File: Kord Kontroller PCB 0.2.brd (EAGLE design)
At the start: 242.5 x 100 mm, 190 parts, among them IC2 74HCT1G125DBV, IC4 ATSAMD51G_TQFN48, J1 MIDIOUTB, J2 MIDIOUTA, SW1 SPST_TACT-KMR2, U1 AP2112K-3.3, U2 ATSAMD51J19A-AUT, X3 microUSB

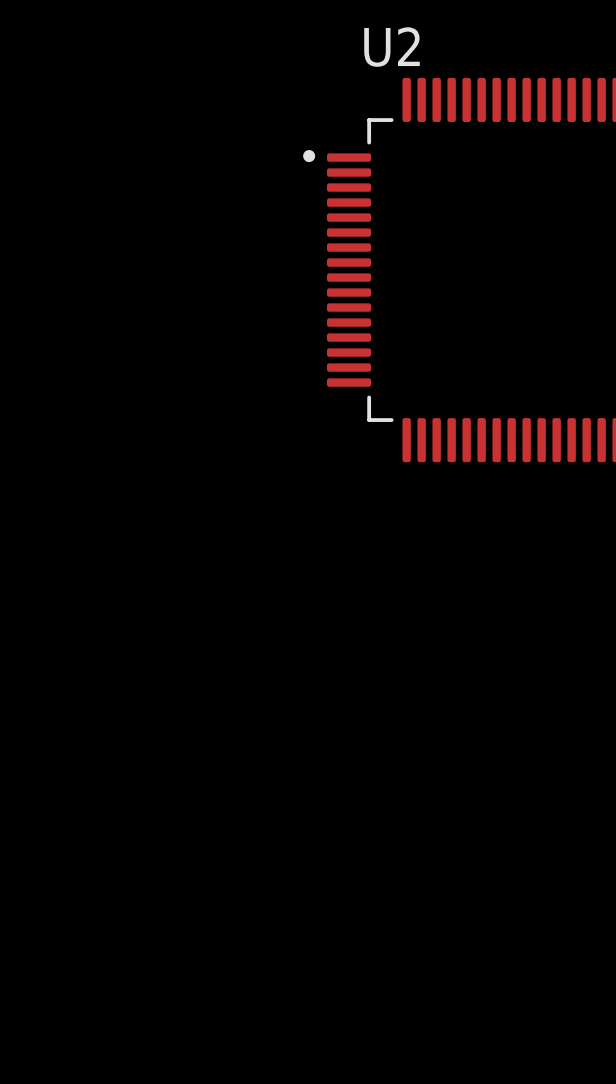
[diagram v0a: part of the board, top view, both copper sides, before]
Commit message: Added lines to new 64-QFN part
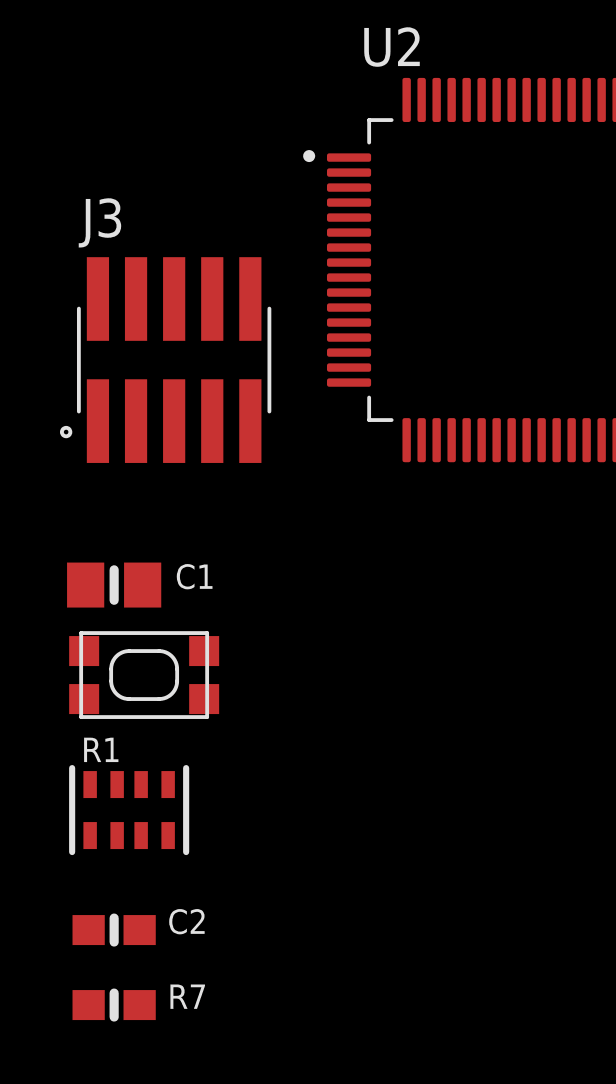
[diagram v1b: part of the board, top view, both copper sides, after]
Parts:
- added C1: 10uF, microbuilder:0805-NO
- added C2: 0.1uF, microbuilder:0603-NO
- added J3: FTSH-105-01-L-DV-KJ, FTSH-105-01-L-DV-K:SAMTEC_FTSH-105-01-L-DV-K
- added R1: 10K, microbuilder:RESPACK_4X0603
- added R7: 10K, microbuilder:0603-NO
- added SW2: SPST_TACT-KMR2, adafruit:KMR2
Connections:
- removed net VDDANA: U2.8
- removed net VDDIO: U2.21, U2.34, U2.48, U2.56
- new net NRESET: C2.2, J3.10, R1.1, SW2.1, SW2.3, U2.52
- new net SWDCLK: J3.4, R7.1, U2.57
- new net SWO: J3.6, U2.59
- new net VDDCORE1: C1.1, U2.53
- net 3.3V: now also J3.1, R1.8, R7.2, U2.21, U2.34, U2.48, U2.56
- net AVDD: now also U2.8
- net COL0: now also U2.1
- net COL1: now also U2.2
- net COL10: now also U2.38
- net COL11: now also U2.41
- net COL12: now also U2.42
- net COL13: now also U2.43
- net COL14: now also U2.44
- net COL2: now also U2.3
- net COL3: now also U2.4
- net COL4: now also U2.13
- net COL5: now also U2.14
- net COL6: now also U2.15
- net COL7: now also U2.35
- net COL8: now also U2.36
- net COL9: now also U2.37
- net D+: now also U2.46
- net D-: now also U2.45
- net GND: now also C1.2, C2.1, J3.3, J3.5, J3.9, SW2.2, SW2.4
- net INT: now also U2.16
- net LEVELSHIFT_3V: now also U2.51
- net MIDIOUTA: now also U2.29
- net MIDIOUTB: now also U2.30
- net ROW0: now also U2.64
- net ROW1: now also U2.63
- net ROW2: now also U2.62
- net ROW3: now also U2.23
- net ROW4: now also U2.24
- net SWDIO: now also J3.2, U2.58
- net VDDCORE: no longer U2.53

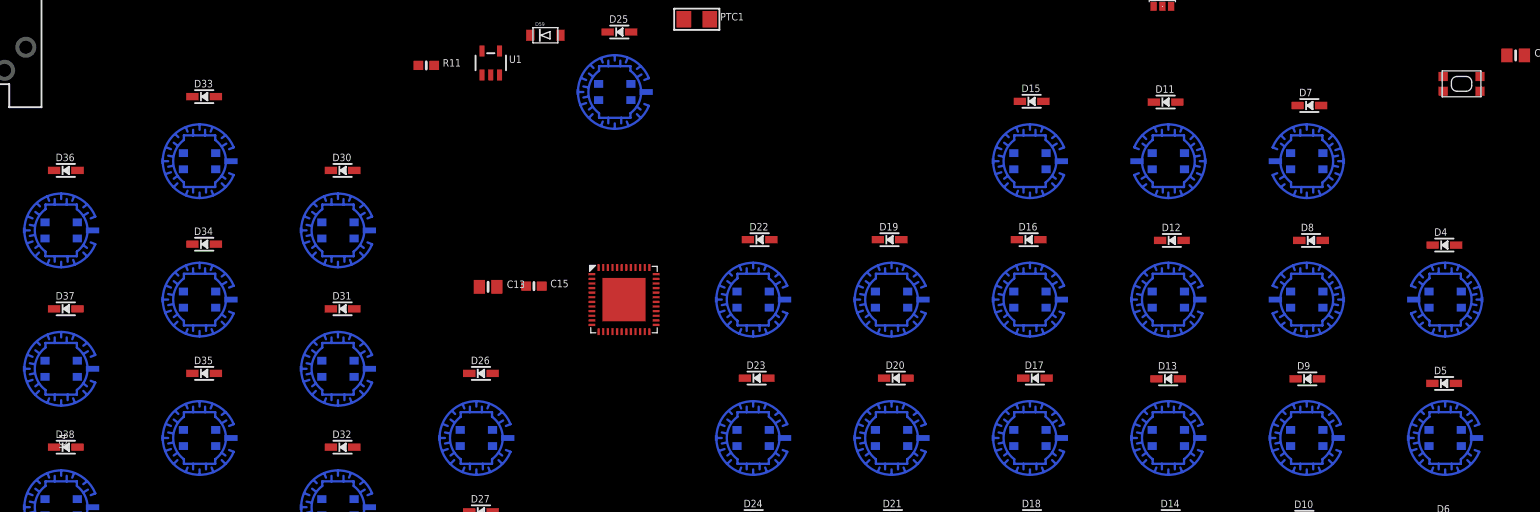
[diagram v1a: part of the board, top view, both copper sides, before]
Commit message: Deleted TQFN8 pin package for 64 pin package
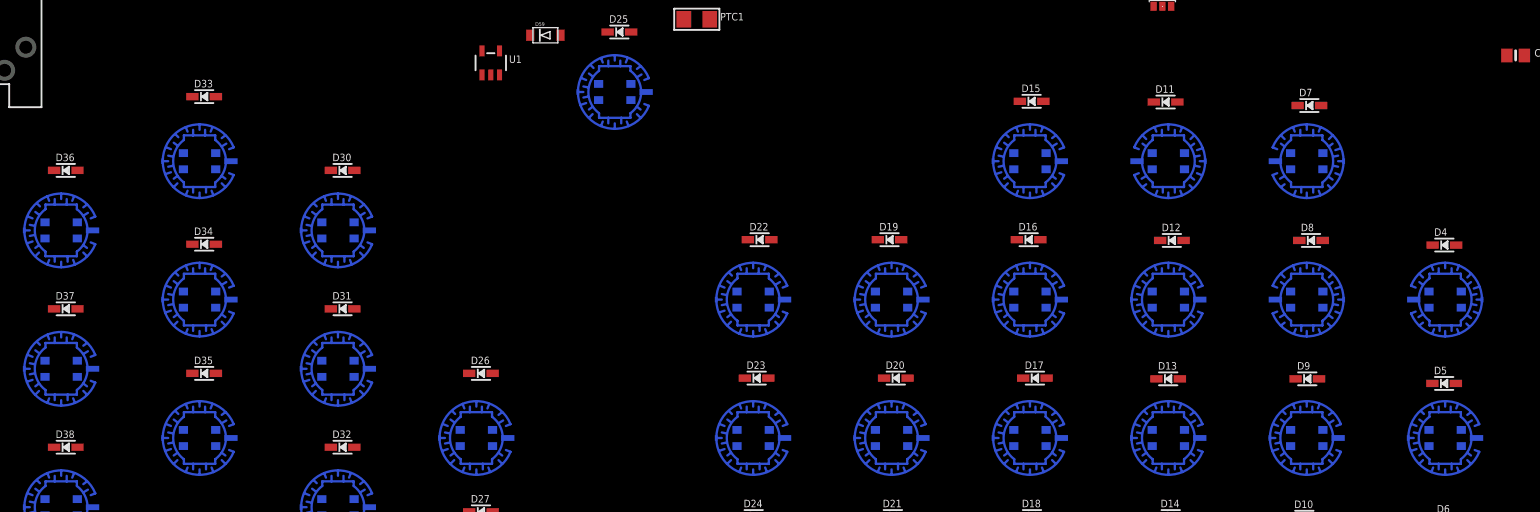
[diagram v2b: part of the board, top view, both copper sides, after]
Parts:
- removed C13: 10uF, microbuilder:0805-NO
- removed C15: 0.1uF, microbuilder:0603-NO
- removed IC4: ATSAMD51G_TQFN48, microbuilder:TQFN48_7MM
- removed R11: 10K, microbuilder:0603-NO
- removed SW1: SPST_TACT-KMR2, adafruit:KMR2
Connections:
- removed net !RESET: C15.2, IC4.40, R2.1, SW1.1, SW1.3
- removed net SWCLK: IC4.45, R11.1
- removed net VDDCORE: C13.1, IC4.41
- removed net VSS: IC4.5
- net 3.3V: no longer IC4.17, IC4.36, IC4.44, R11.2, R2.8
- net AVDD: no longer IC4.6
- net COL0: no longer IC4.1
- net COL1: no longer IC4.2
- net COL10: no longer IC4.27
- net COL11: no longer IC4.28
- net COL12: no longer IC4.29
- net COL13: no longer IC4.30
- net COL14: no longer IC4.31
- net COL2: no longer IC4.3
- net COL3: no longer IC4.4
- net COL4: no longer IC4.10
- net COL5: no longer IC4.11
- net COL6: no longer IC4.12
- net COL7: no longer IC4.13
- net COL8: no longer IC4.25
- net COL9: no longer IC4.26
- net D+: no longer IC4.34
- net D-: no longer IC4.33
- net GND: no longer C13.2, C15.1, IC4.18, IC4.35, IC4.42, IC4.THERMAL, SW1.2, SW1.4
- net INT: no longer IC4.9
- net LEVELSHIFT_3V: no longer IC4.39
- net MIDIOUTA: no longer IC4.21
- net MIDIOUTB: no longer IC4.22
- net ROW0: no longer IC4.47
- net ROW1: no longer IC4.48
- net ROW2: no longer IC4.37
- net ROW3: no longer IC4.38
- net ROW4: no longer IC4.24
- net SCL: no longer IC4.8
- net SDA: no longer IC4.7
- net SWDIO: no longer IC4.46
- net VSW: no longer IC4.43

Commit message: traced routes for LEDs and half the board
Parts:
- removed JP3, JP4: (no value), microbuilder:5P_EDGECONNECT
- removed R2: 10K, microbuilder:RESPACK_4X0603
- moved SW2 304.9 mm to (167.0, 97.0)
- moved C2 298.6 mm to (158.0, 92.0)
- moved R7 296.3 mm to (156.0, 88.5)
- moved C1 282.9 mm to (147.0, 87.5)
- moved J3 282.2 mm to (148.5, 94.5), flipped to the bottom
- moved R1 282.2 mm to (146.5, 81.0)
- moved U2 238.6 mm to (127.0, 50.5), flipped to the bottom
- moved B29 60.5 mm to (127.5, 15.0), turned to 180 degrees
- moved C9 59.7 mm to (165.6, 91.0)
- moved B32 27.0 mm to (97.5, 37.5)
- moved C10 25.6 mm to (137.3, 87.0)
- moved U1 23.8 mm to (137.6, 82.2)
- moved IC2 22.5 mm to (209.3, 93.1)
- moved B28 21.2 mm to (112.5, 22.5), turned to 180 degrees
- moved C11 19.4 mm to (137.4, 91.4)
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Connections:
- removed net N$104: LED50.3, LED52.1
- removed net N$105: LED51.1, LED52.3
- removed net N$106: LED51.3, LED53.1
- removed net N$90: LED34.3, LED36.1
- removed net N$91: LED35.1, LED36.3
- removed net N$92: LED35.3, LED37.1
- removed net N$97: LED42.3, LED44.1
- removed net N$98: LED43.1, LED44.3
- removed net N$99: LED43.3, LED45.1
- removed net SCL: JP3.4, JP4.4, R2.4
- removed net SDA: JP3.5, JP4.5, R2.3
- new net N$3: LED36.3, LED37.1
- new net N$49: LED34.3, LED35.1
- new net N$50: LED35.3, LED36.1
- new net N$51: LED44.3, LED45.1
- new net N$55: LED43.3, LED44.1
- new net N$59: LED42.3, LED43.1
- new net N$65: LED50.3, LED51.1
- new net N$67: LED51.3, LED52.1
- new net N$68: LED52.3, LED53.1
- net 3.3V: no longer R2.5, R2.6, R2.7
- net GND: no longer JP3.3, JP4.3
- net INT: no longer JP3.1, JP4.1, R2.2
- net N$30: now also LED11.1; no longer LED12.1
- net N$31: now also LED11.3, LED12.1; no longer LED11.1, LED12.3
- net N$32: now also LED12.3; no longer LED11.3
- net N$42: now also LED27.1; no longer LED28.1
- net N$43: now also LED29.1; no longer LED27.1
- net N$44: now also LED28.1; no longer LED29.1
- net VDD: no longer JP3.2, JP4.2
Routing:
- net ROW3: track 0.00 -> 150.0 mm, vias 0 -> 7
- net ROW1: track 0.00 -> 141.7 mm, vias 0 -> 8
- net ROW2: track 0.00 -> 140.0 mm, vias 0 -> 9
- net ROW0: track 0.00 -> 104.2 mm, vias 0 -> 3
- net N$45: track 0.00 -> 96.5 mm, vias 0 -> 4
- net N$17: track 0.00 -> 66.1 mm, vias 0 -> 2
- net LEVELSHIFT_5V: track 0.00 -> 65.3 mm, vias 0 -> 1
- net N$30: track 0.00 -> 64.8 mm, vias 0 -> 2
- net N$34: track 0.00 -> 63.6 mm, vias 0 -> 2
- net N$103: track 0.00 -> 63.5 mm, vias 0 -> 4
- net N$100: track 0.00 -> 62.5 mm, vias 0 -> 4
- net N$113: track 0.00 -> 58.8 mm, vias 0 -> 4
- net N$95: track 0.00 -> 55.6 mm, vias 0 -> 4
- net N$40: track 0.00 -> 54.7 mm, vias 0 -> 2
- net N$8: track 0.00 -> 49.4 mm, vias 0 -> 2
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- added copper zone on layer 1, net GND
- added copper zone on layer 16, net VDD
- removed copper zone on layer 16, net GND

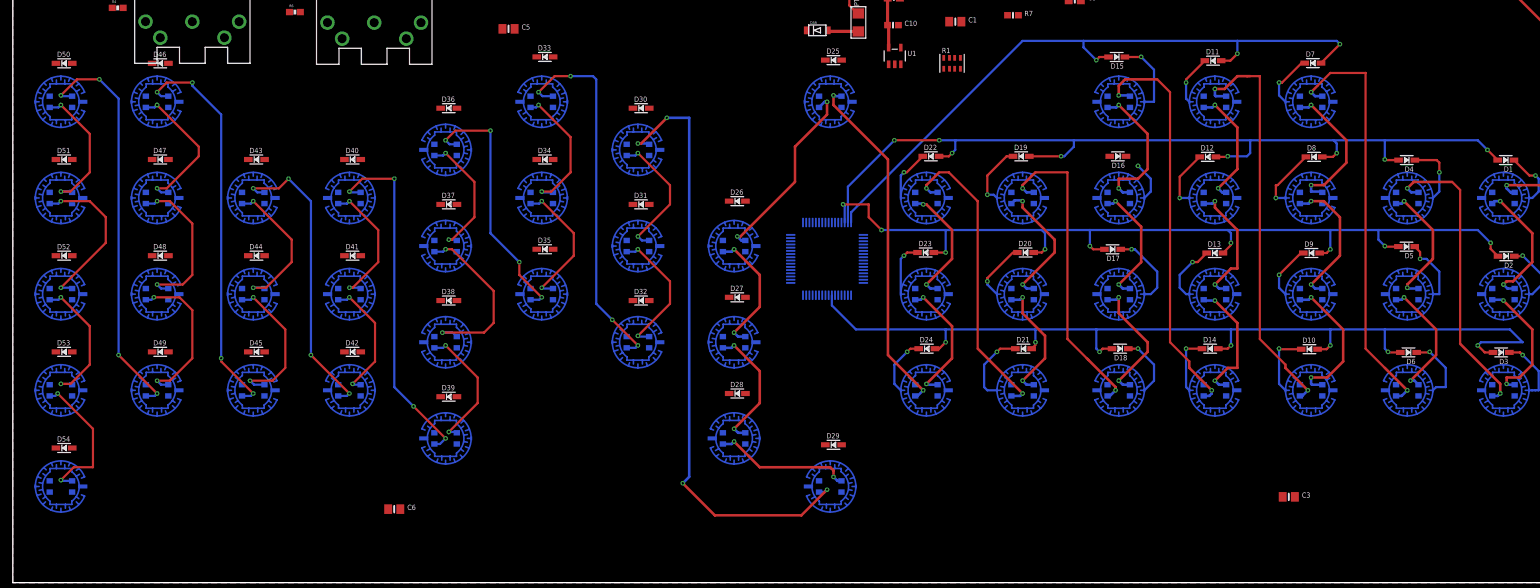
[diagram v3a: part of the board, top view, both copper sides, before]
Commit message: Added Routes for Cols 0-6, Finished Rows and diodes
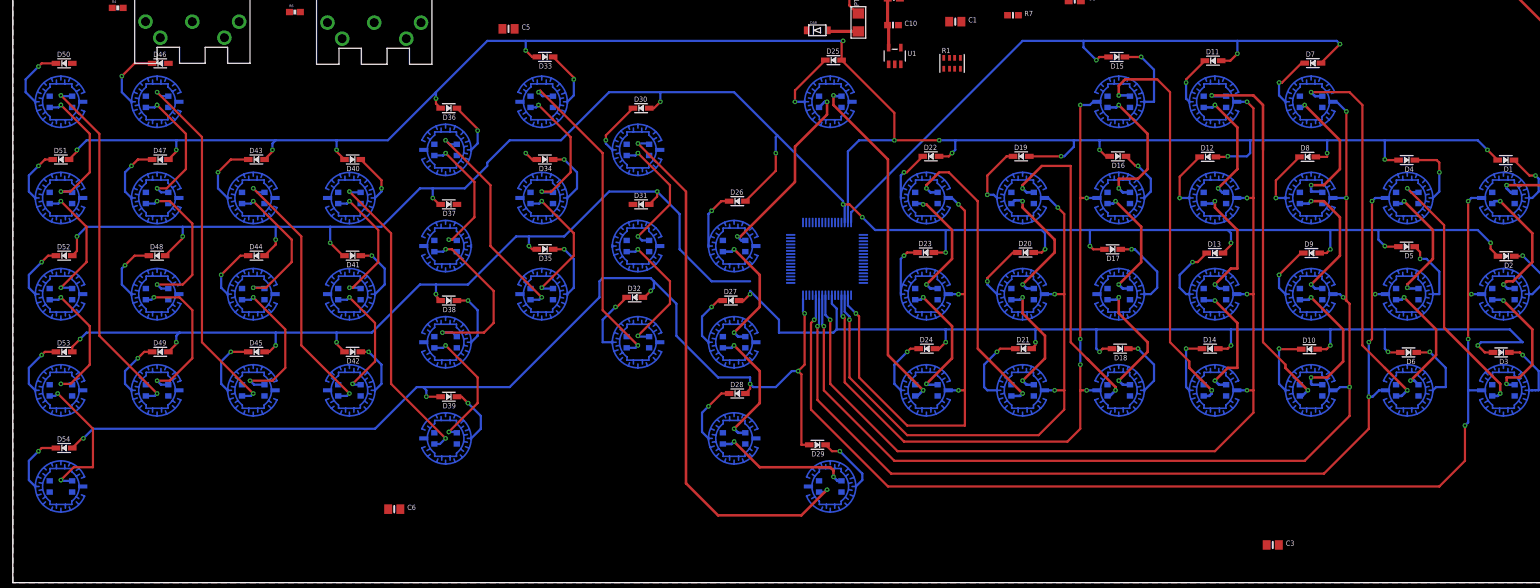
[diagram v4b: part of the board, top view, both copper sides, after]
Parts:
- moved C3 7.91 mm to (196.5, 5.88)
- moved D29 2.50 mm to (125.5, 21.5), turned to 180 degrees
- moved D27 1.12 mm to (112.0, 44.0)
- moved D32 1.12 mm to (97.0, 44.5)
- moved D8 1.00 mm to (202.0, 66.4)
- moved D48 0.50 mm to (22.5, 51.0)
- moved D51 0.50 mm to (7.50, 66.0)
- turned B28 to 0 degrees
- turned D33 to 180 degrees
- turned D34 to 180 degrees
- turned D35 to 180 degrees
- turned D36 to 180 degrees
- turned D37 to 180 degrees
- turned D38 to 180 degrees
- turned D39 to 180 degrees
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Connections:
- net COL0: now also U2.28; no longer U2.1
- net COL1: now also U2.27; no longer U2.2
- net COL2: now also U2.26; no longer U2.3
- net COL3: now also U2.25; no longer U2.4
- net COL4: now also U2.20; no longer U2.13
- net COL5: now also U2.19; no longer U2.14
- net COL6: now also U2.18; no longer U2.15
- net ROW1: no longer D29.A
- net ROW4: now also D29.A, U2.32; no longer U2.24
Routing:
- net ROW2: track 140.0 -> 316.4 mm, vias 9 -> 17
- net COL0: track 0.00 -> 173.4 mm, vias 0 -> 5
- net ROW1: track 141.7 -> 312.9 mm, vias 8 -> 16
- net ROW4: track 0.00 -> 171.1 mm, vias 0 -> 6
- net ROW3: track 150.0 -> 317.2 mm, vias 7 -> 15
- net COL2: track 0.00 -> 161.0 mm, vias 0 -> 5
- net COL1: track 0.00 -> 152.6 mm, vias 0 -> 5
- net COL3: track 0.00 -> 144.7 mm, vias 0 -> 5
- net COL4: track 0.00 -> 113.3 mm, vias 0 -> 6
- net COL5: track 0.00 -> 92.9 mm, vias 0 -> 4
- net COL6: track 0.00 -> 74.7 mm, vias 0 -> 4
- net N$45: track 96.5 -> 85.0 mm, vias 4 -> 2
- net N$132: track 0.00 -> 10.2 mm, vias 0 -> 1
- net N$117: track 0.00 -> 10.2 mm, vias 0 -> 1
- net N$120: track 0.00 -> 10.2 mm, vias 0 -> 1
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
